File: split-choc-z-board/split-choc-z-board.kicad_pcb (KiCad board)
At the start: 2 copper layers, 43 parts, among them SW1 SW_SPST, SW10 SW_SPST, SW11 SW_SPST, SW12 SW_SPST, SW13 SW_SPST, SW14 SW_SPST, SW15 SW_SPST, SW16 SW_SPST, SW17 SW_SPST, SW18 SW_SPST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

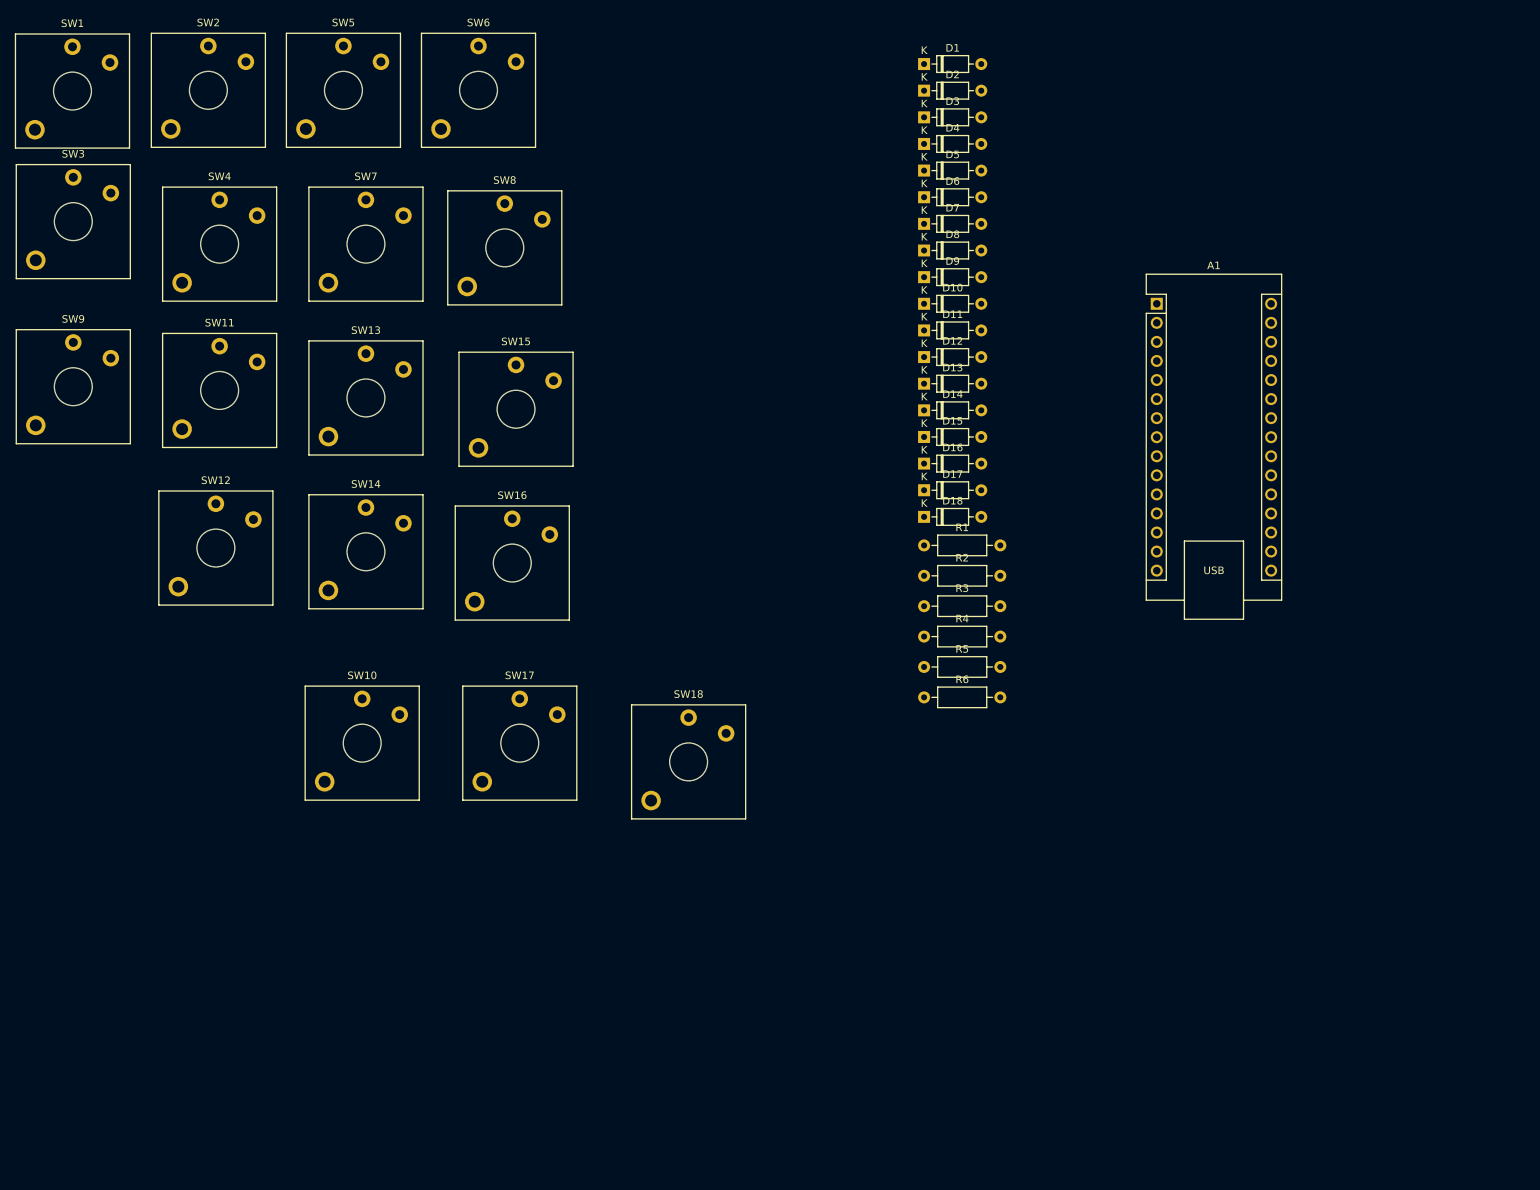
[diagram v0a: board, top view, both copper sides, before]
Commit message: Changed TTRS to USB C
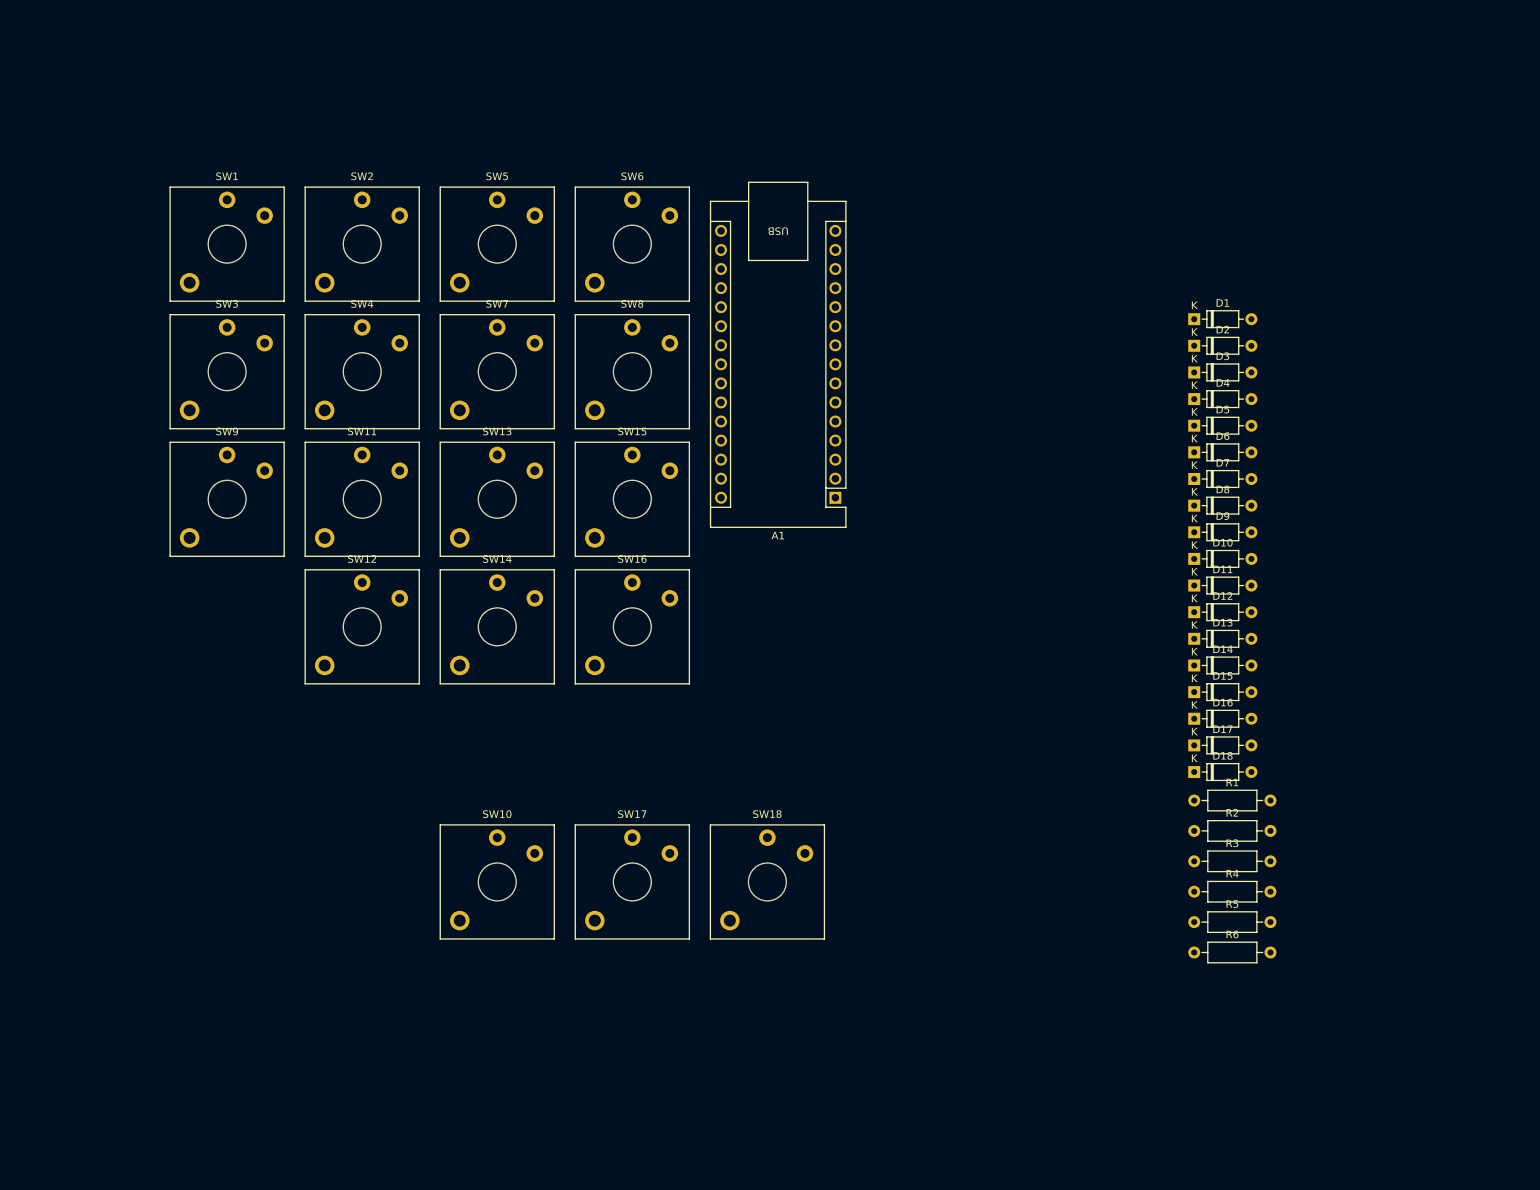
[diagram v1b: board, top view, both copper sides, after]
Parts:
- moved A1 50.0 mm to (135.1, 84.8), turned to 180 degrees
- moved D4 49.5 mm to (182.9, 71.7)
- moved D9 49.5 mm to (182.9, 89.4)
- moved R4 49.5 mm to (182.9, 137.3)
- moved D1 49.5 mm to (182.9, 61.0)
- moved D10 49.5 mm to (182.9, 93.0)
- moved D11 49.5 mm to (182.9, 96.5)
- moved D12 49.5 mm to (182.9, 100.0)
- moved D13 49.5 mm to (182.9, 103.6)
- moved D14 49.5 mm to (182.9, 107.2)
- moved D15 49.5 mm to (182.9, 110.7)
- moved D16 49.5 mm to (182.9, 114.2)
- moved D17 49.5 mm to (182.9, 117.8)
- moved D18 49.5 mm to (182.9, 121.3)
- moved D2 49.5 mm to (182.9, 64.5)
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
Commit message: Update: Added more footprints 🚀
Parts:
- added P2: USB_C_Plug_USB2.0, Library:GCT_USB4105-GF-A, F.Cu at (151.7, 164.2)
- added R1: 5.1k, Resistor_THT:R_Axial_DIN0207_L6.3mm_D2.5mm_P10.16mm_Horizontal, F.Cu at (147.7, 169.6)
- added R2: 5.1k, Resistor_THT:R_Axial_DIN0207_L6.3mm_D2.5mm_P10.16mm_Horizontal, F.Cu at (147.7, 173.7)
- added U1: USBLC6-2SC6, Package_TO_SOT_SMD:SOT-23-6, F.Cu at (162.0, 170.0)
- D1, D10, D11, D12, D13, D14, D15, D16, D17, D18, D2, D3, D4, D5, D6, D7, D8, D9: footprint Diode_THT:D_DO-35_SOD27_P7.62mm_Horizontal -> footprints:SOD123_MCC
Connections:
- A1 pad 1: unconnected-(A1-TX1-Pad1) -> /TX
- A1 pad 2: unconnected-(A1-RX1-Pad2) -> /RX
- A1 pad 23: /SDA -> unconnected-(A1-SDA/A4-Pad23)
- A1 pad 24: /SCL -> unconnected-(A1-SCL/A5-Pad24)

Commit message: Adding more to pcb
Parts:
- removed P2: USB_C_Plug_USB2.0, Library:GCT_USB4105-GF-A
- added J1: USB4105-GF-A, Library:GCT_USB4105-GF-A, F.Cu at (151.7, 95.5)
- moved SW12 74.3 mm to (126.0, 51.0)
- moved SW14 49.5 mm to (126.0, 68.0)
- moved D1 33.1 mm to (216.0, 61.0)
- moved D10 33.1 mm to (216.0, 93.0)
- moved D11 33.1 mm to (216.0, 96.5)
- moved D12 33.1 mm to (216.0, 100.0)
- moved D13 33.1 mm to (216.0, 103.6)
- moved D14 33.1 mm to (216.0, 107.2)
- moved D15 33.1 mm to (216.0, 110.7)
- moved D16 33.1 mm to (216.0, 114.2)
- moved D17 33.1 mm to (216.0, 117.8)
- moved D18 33.1 mm to (216.0, 121.3)
- moved D2 33.1 mm to (216.0, 64.5)
- moved D3 33.1 mm to (216.0, 68.1)
- moved D4 33.1 mm to (216.0, 71.7)
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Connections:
- R1 pad 1: Net-(P2-CC) -> GND
- R1 pad 2: GND -> /CC1
- R2 pad 1: GND -> /CC2
- R2 pad 2: Net-(P2-VCONN) -> GND

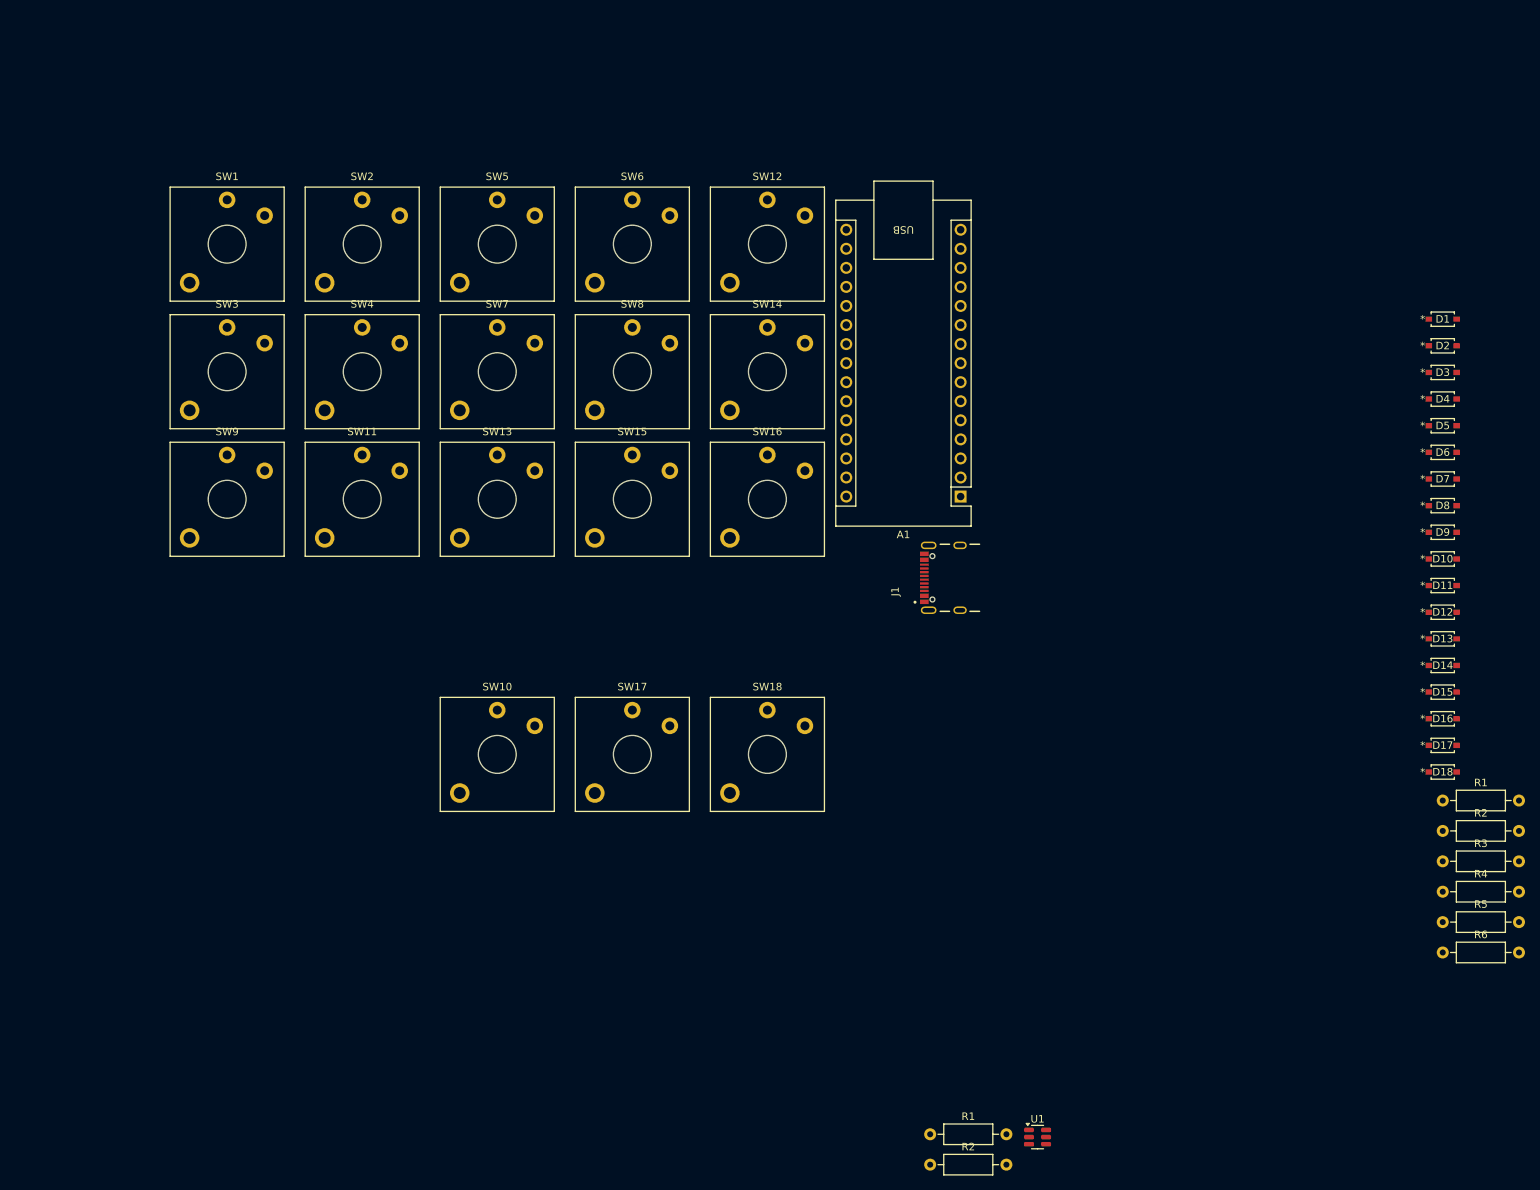
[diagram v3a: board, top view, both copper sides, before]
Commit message: Finalized placement of components 🎉 and defined edge
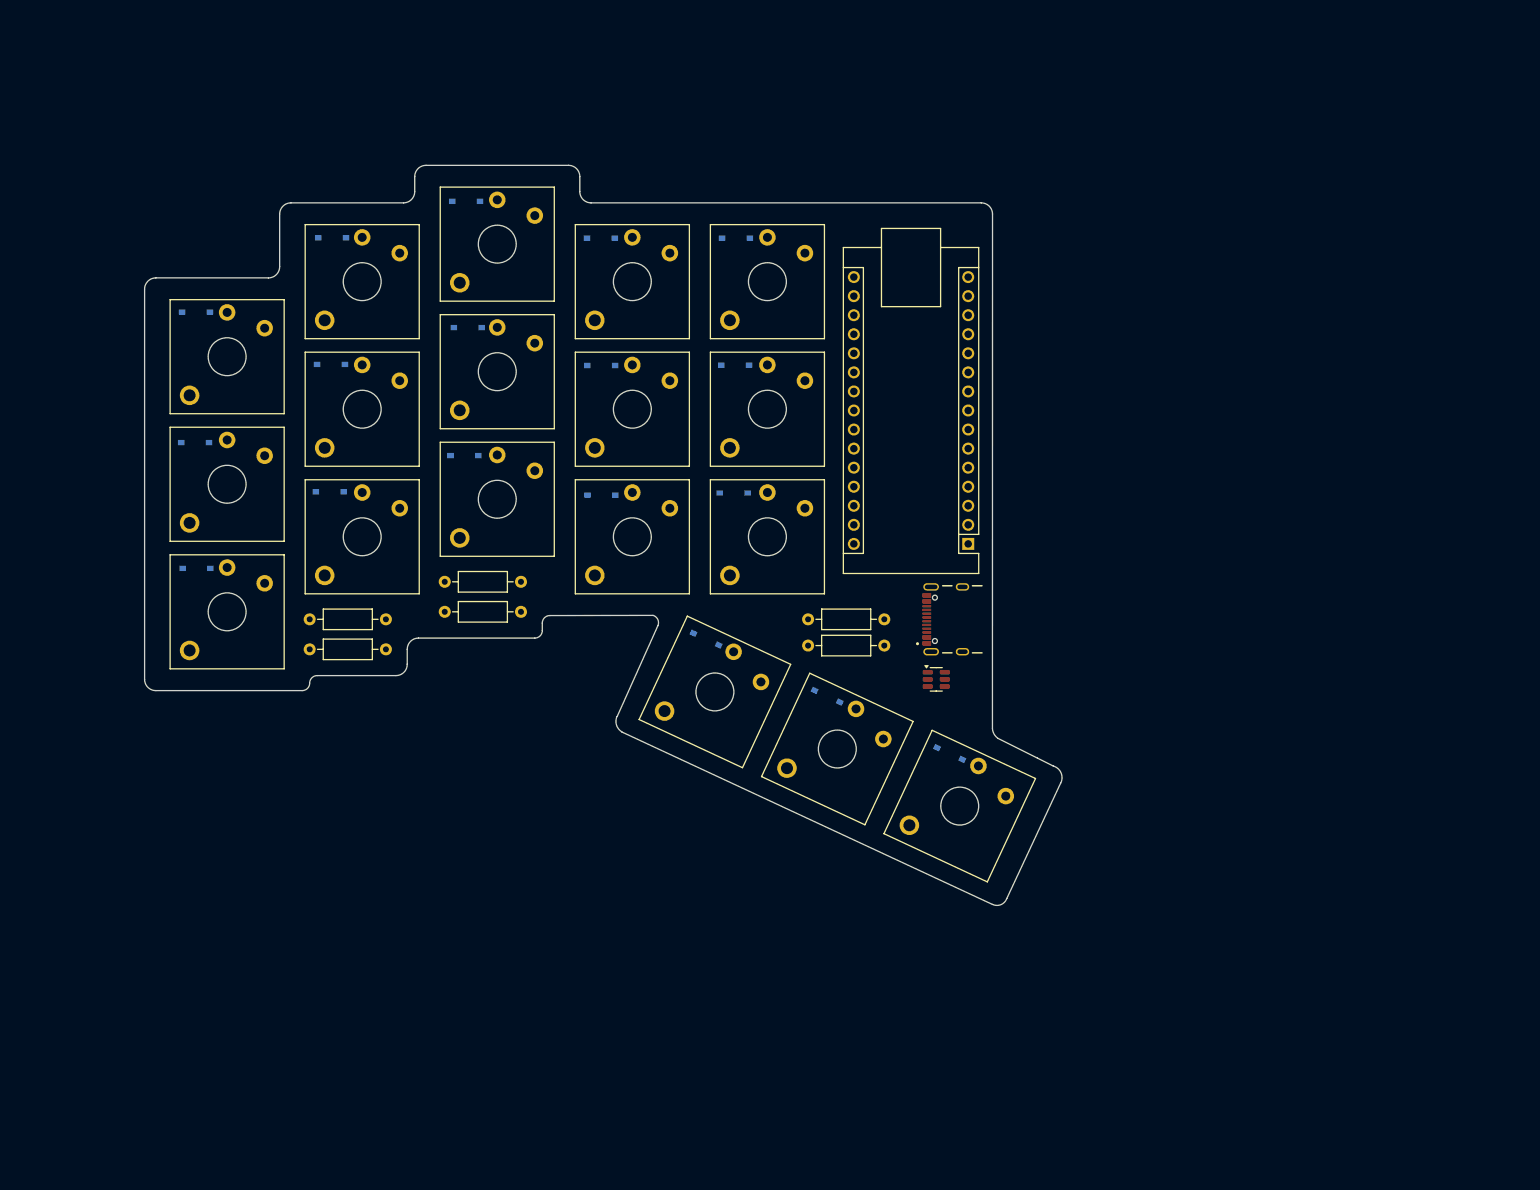
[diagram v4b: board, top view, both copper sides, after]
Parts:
- removed the R1 at (216.0, 125.2)
- removed the R2 at (216.0, 129.2)
- D1, D10, D11, D12, D13, D14, D15, D16, D17, D18, D2, D3, D4, D5, D6, D7, D8, D9: moved to B.Cu
- moved D3 166.5 mm to (49.7, 77.5)
- moved D1 166.2 mm to (49.9, 60.0)
- moved D9 166.1 mm to (49.9, 94.2)
- moved R4 154.4 mm to (65.0, 105.0)
- moved R3 154.4 mm to (65.0, 101.0)
- moved D11 148.8 mm to (67.7, 84.0)
- moved D2 148.7 mm to (68.0, 50.1)
- moved D4 148.2 mm to (67.8, 67.0)
- moved R6 140.5 mm to (83.0, 100.0)
- moved R5 140.5 mm to (83.0, 96.0)
- moved D5 133.5 mm to (85.8, 45.3)
- moved D13 132.6 mm to (85.6, 79.2)
- moved D7 131.5 mm to (86.1, 62.1)
- moved D6 115.8 mm to (103.8, 50.2)
- moved D15 115.2 mm to (103.9, 84.5)
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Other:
- board outline added: 122.3 x 98.6 mm
